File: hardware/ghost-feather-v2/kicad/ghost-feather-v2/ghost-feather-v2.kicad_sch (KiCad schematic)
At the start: 33 parts, among them J1 Conn_ARM_SWD_TagConnect_TC203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, SW1 BOOT0, U1 STM32F722RETx, U2 BMI088, U3 IIS2MDCTR, U4 BMP390, U5 STM32F722RETx

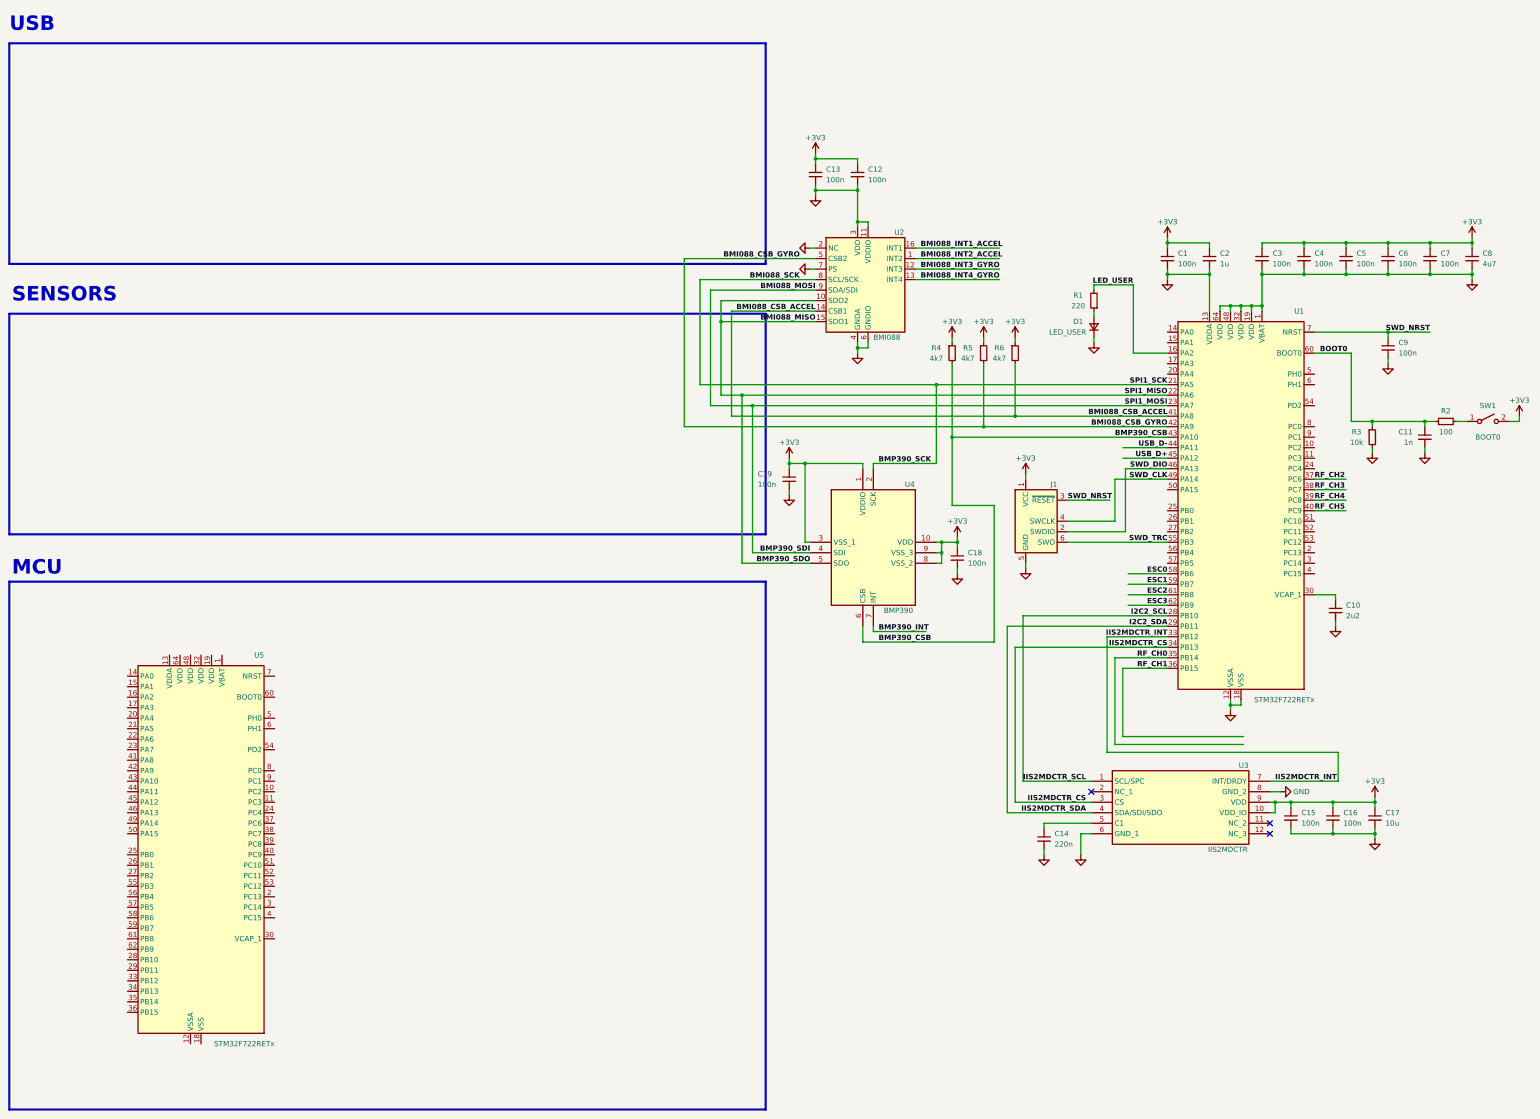
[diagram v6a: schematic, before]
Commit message: feat: hardware: Finish SENSORS and MCU sectors on schematic
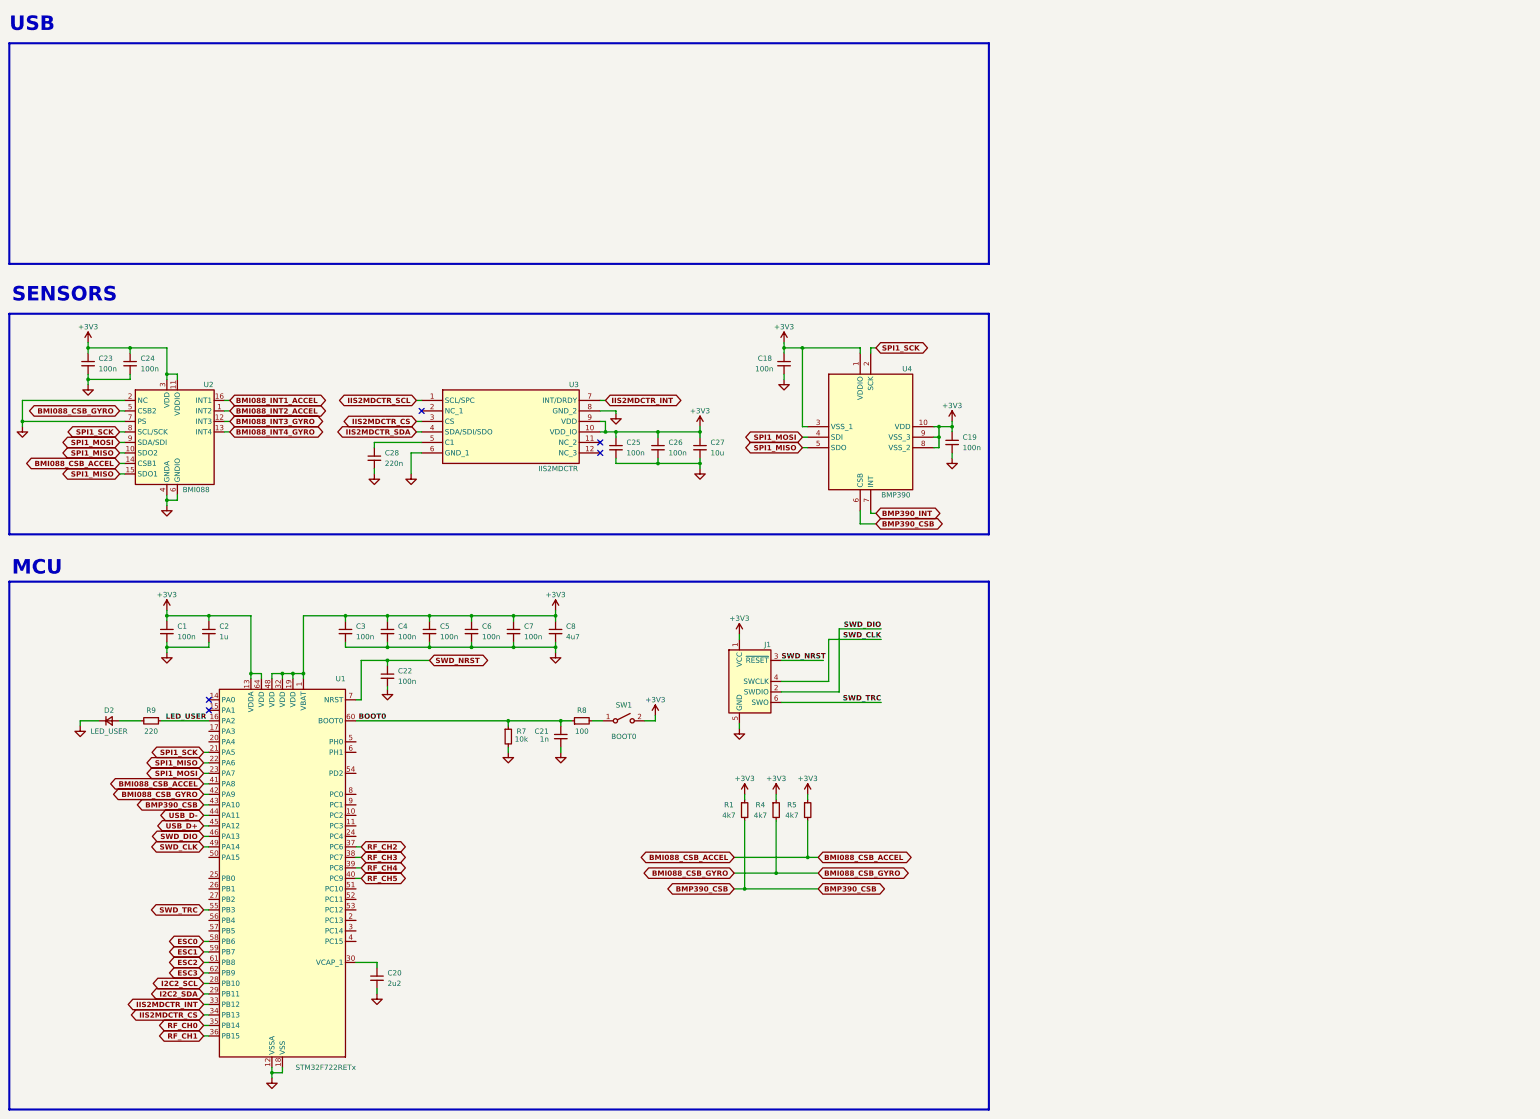
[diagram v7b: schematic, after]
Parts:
- removed C10: 2u2, symbol Device:C_Small
- removed C11: 1n, symbol Device:C_Small
- removed C12, C13, C15, C16, C9: 100n, symbol Device:C_Small
- removed C14: 220n, symbol Device:C_Small
- removed C17: 10u, symbol Device:C_Small
- removed D1: LED_USER, symbol Device:D_Small
- removed R2: 100, symbol Device:R_Small
- removed R3: 10k, symbol Device:R_Small
- removed R6: 4k7, symbol Device:R_Small
- removed U1: STM32F722RETx, Package_QFP:LQFP-64_10x10mm_P0.5mm, symbol MCU_ST_STM32F7:STM32F722RETx
- added C20: 2u2, symbol Device:C_Small
- added C21: 1n, symbol Device:C_Small
- added C22, C23, C24, C25, C26: 100n, symbol Device:C_Small
- added C27: 10u, symbol Device:C_Small
- added C28: 220n, symbol Device:C_Small
- added D2: LED_USER, symbol Device:D_Small
- added R7: 10k, symbol Device:R_Small
- added R8: 100, symbol Device:R_Small
- added R9: 220, symbol Device:R_Small
- R1: value 220 -> 4k7
- renumbered U5 to U1
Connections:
- net BMI088_MISO is gone; now on net SPI1_MISO: U2.10 (SDO2), U2.15 (SDO1), U4.5 (SDO)
- net BMI088_MOSI is gone; now on net SPI1_MOSI: U2.9 (SDA/SDI), U4.4 (SDI)
- net BMI088_SCK is gone; now on net SPI1_SCK: U2.8 (SCL/SCK), U4.2 (SCK)
- net +3V3: now also R1.1, U1.1 (VBAT), U1.13 (VDDA), U1.19 (VDD), U1.32 (VDD), U1.48 (VDD), U1.64 (VDD), U2.11 (VDDIO), U2.3 (VDD), C23.1, C24.1, C25.1, C26.1, C27.1
- net BMI088_CSB_ACCEL: now also R5.2, U1.41 (PA8)
- net BMI088_CSB_GYRO: now also R4.2, U1.42 (PA9); no longer R5.2
- net BMP390_CSB: now also R1.2, U1.43 (PA10); no longer R4.2
- net BOOT0: now also U1.60 (BOOT0), C21.1, R7.1, R8.1
- net ESC0: now also U1.58 (PB6)
- net ESC1: now also U1.59 (PB7)
- net ESC2: now also U1.61 (PB8)
- net ESC3: now also U1.62 (PB9)
- net GND: now also U1.12 (VSSA), U1.18 (VSS), U1.31 (VSS), U1.47 (VSS), U1.63 (VSS), C20.2, C21.2, C22.2, C23.2, C24.2, C25.2, C26.2, C27.2, C28.2, D2.1 (K), R7.2; no longer U2.11 (VDDIO), U2.3 (VDD)
- net I2C2_SCL: now also U1.28 (PB10); no longer U3.1 (SCL/SPC)
- net I2C2_SDA: now also U1.29 (PB11); no longer U3.4 (SDA/SDI/SDO)
- net IIS2MDCTR_CS: now also U1.34 (PB13)
- net IIS2MDCTR_INT: now also U1.33 (PB12)
- net LED_USER: now also U1.16 (PA2), R9.1; no longer R1.2
- net RF_CH0: now also U1.35 (PB14)
- net RF_CH1: now also U1.36 (PB15)
- net RF_CH2: now also U1.37 (PC6)
- net RF_CH3: now also U1.38 (PC7)
- net RF_CH4: now also U1.39 (PC8)
- net RF_CH5: now also U1.40 (PC9)
- net SWD_CLK: now also U1.49 (PA14)
- net SWD_DIO: now also U1.46 (PA13)
- net SWD_NRST: now also U1.7 (NRST), C22.1
- net SWD_TRC: now also U1.55 (PB3)
- net USB_D+: now also U1.45 (PA12)
- net USB_D-: now also U1.44 (PA11)
- net at U3.5 (C1): now also C28.1
- net at SW1.1 (A): now also R8.2
- net SPI1_SCK: now reaches U1.21 (PA5)
- net SPI1_MISO: now reaches U1.22 (PA6)
- net SPI1_MOSI: now reaches U1.23 (PA7)
- net at U1.30 (VCAP_1): now also C20.1
- new net: D2.2 (A), R9.2
- new net IIS2MDCTR_SCL: U3.1 (SCL/SPC)
- new net IIS2MDCTR_SDA: U3.4 (SDA/SDI/SDO)
- no-connect marks 3 -> 5
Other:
- moved on the sheet: U1

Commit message: feat: hardware: wip: Add nRF52810
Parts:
- added C10: 4u7, symbol Device:C_Small
- added C11, C12, C9: 100n, symbol Device:C_Small
- added C13: 100p, symbol Device:C_Small
- added C14: 1u, symbol Device:C_Small
- added C15: 0p8, symbol Device:C_Small
- added J2: nRF52810, Connector:Tag-Connect_TC2030-IDC-NL_2x03_P1.27mm_Vertical, symbol Connector:Conn_ARM_SWD_TagConnect_TC2030-NL
- added L1: 3n9, symbol Device:L_Small
- added U2: nRF52810-QCxx, Package_DFN_QFN:QFN-32-1EP_5x5mm_P0.5mm_EP3.6x3.6mm, symbol MCU_Nordic:nRF52810-QCxx
- J1: value Conn_ARM_SWD_TagConnect_TC2030-NL -> STM32F722RETx
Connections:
- net +3V3: now also C10.1, C11.1, C9.1, J2.1 (VCC), U2.25 (VDD), U2.32 (VDD), U2.9 (VDD)
- net GND: now also C10.2, C11.2, C12.2, C13.2, C14.2, C15.2, C9.2, J2.5 (GND), U2.20 (VSS), U2.29 (VSS), U2.33 (VSS)
- net SWD_CLK renamed STM32_SWD_CLK
- net SWD_DIO renamed STM32_SWD_DIO
- net SWD_NRST renamed STM32_SWD_NRST
- net SWD_TRC renamed STM32_SWD_TRC
- new net: C12.1, U2.1 (DEC1)
- new net: C15.1, L1.2, U2.19 (ANT)
- new net: C13.1, U2.22 (DEC3)
- new net: C14.1, U2.30 (DEC4)
- new net NFR_SWD_CLK: J2.4 (SWCLK), U2.17 (SWDCLK)
- new net NRF_SWD_DIO: J2.2 (SWDIO), U2.18 (SWDIO)
- no-connect marks 5 -> 9
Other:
- moved on the sheet: R1, R4, R5
